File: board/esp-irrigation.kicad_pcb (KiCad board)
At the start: 2 copper layers, 23 parts, among them J1 ESP01_Header, J2 AC IN, J3 Valves, U1 MCP23008-xSO, U2 SMDA36-7, U3 LM2594HVM-3.3

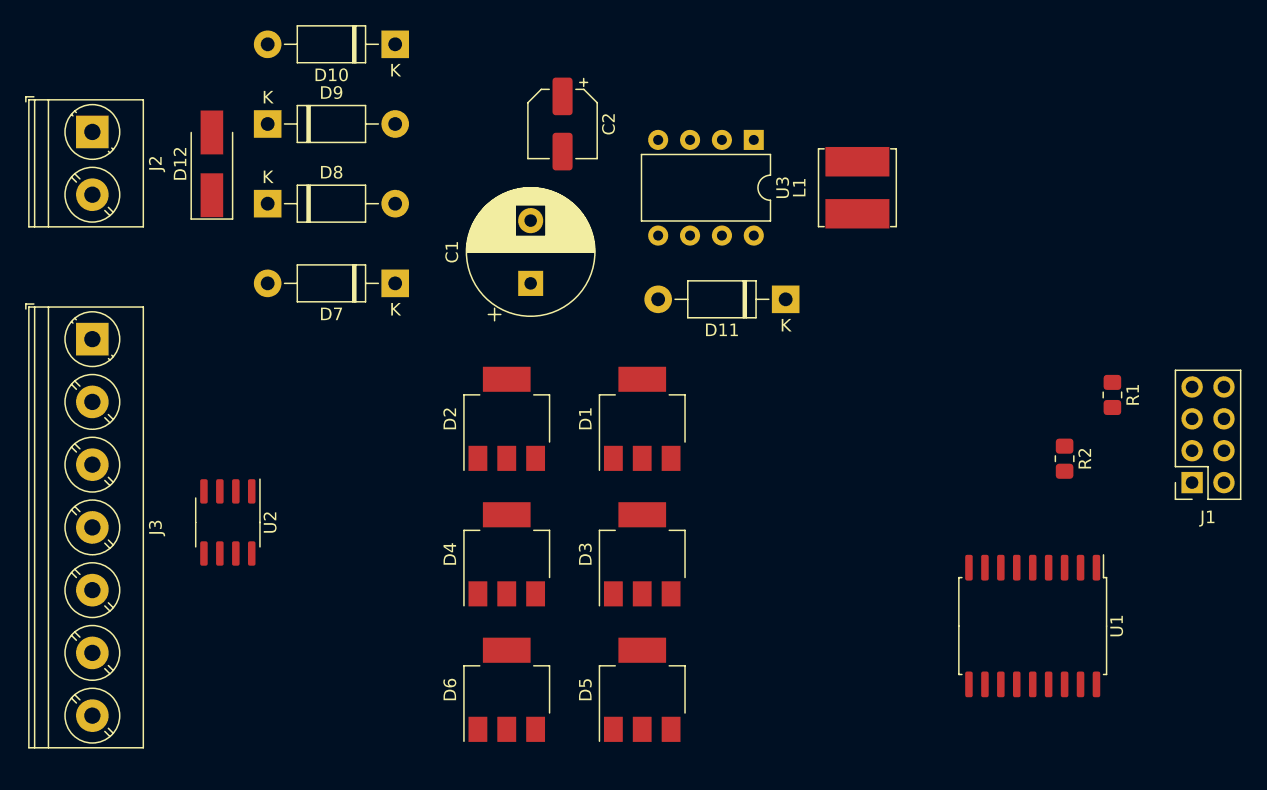
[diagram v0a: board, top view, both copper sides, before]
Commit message: add indicator leds
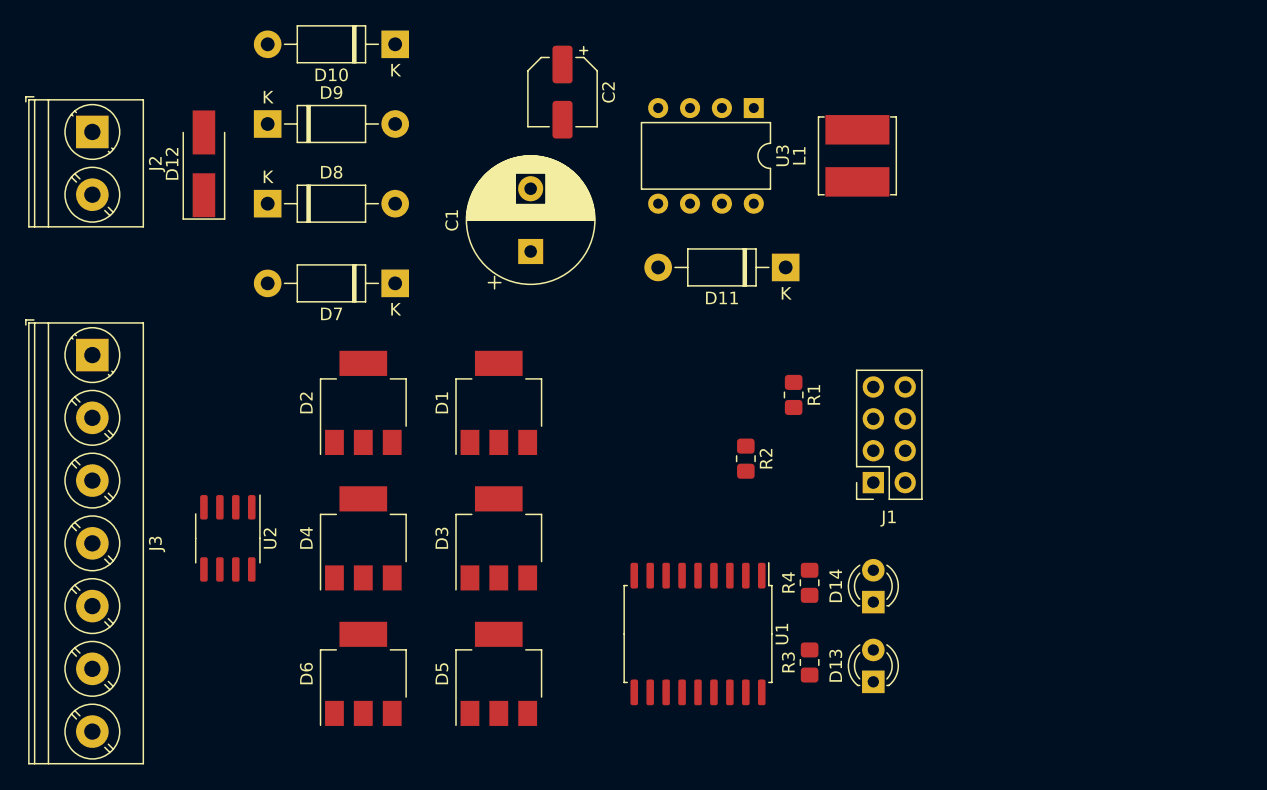
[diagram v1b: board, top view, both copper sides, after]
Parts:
- added D13: LED Red, LED_THT:LED_D3.0mm, F.Cu at (87.6, 68.6)
- added D14: LED Green, LED_THT:LED_D3.0mm, F.Cu at (87.6, 62.2)
- added R3: 100, Resistor_SMD:R_0805_2012Metric_Pad1.20x1.40mm_HandSolder, F.Cu at (82.5, 67.0)
- added R4: 47, Resistor_SMD:R_0805_2012Metric_Pad1.20x1.40mm_HandSolder, F.Cu at (82.5, 60.7)
- moved U1 26.7 mm to (73.7, 64.8)
- moved J1 25.4 mm to (87.6, 52.7)
- moved R1 25.4 mm to (81.3, 45.7)
- moved R2 25.4 mm to (77.5, 50.8)
- moved D5 11.5 mm to (57.8, 67.9)
- moved D1 11.5 mm to (57.8, 46.4)
- moved D3 11.5 mm to (57.8, 57.1)
- moved D6 11.5 mm to (47.0, 67.9)
- moved D2 11.5 mm to (47.0, 46.4)
- moved D4 11.5 mm to (47.0, 57.1)
- moved C1 2.54 mm to (60.3, 34.3)
- moved C2 2.54 mm to (62.9, 21.6)
- moved D11 2.54 mm to (80.6, 35.6)
- moved L1 2.54 mm to (86.4, 26.7)
- moved U3 2.54 mm to (78.1, 22.9)
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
